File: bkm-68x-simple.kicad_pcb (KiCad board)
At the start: 2 copper layers, 230.4 x 233.5 mm, 250 parts, among them CN985 mezz-conn-02x50, CN986 mezz-conn-02x50, J1 PR_R, J10 TP_VIDEO_OE, J11 TP_VSYNC, J12 JTAG, J13 PR_R_OUT, J14 VSYNC_DISCRETE, J15 Y_G_OUT, J16 PB_B_OUT, J17 EXT_SYNC_OUT, J18 Conn_01x02_Male, J19 TP_NORM_Y_G, J2 Y_G, J20 TP_RGB_COMP_X, J21 TP_HD_SD_X, J3 PB_B, J4 EXT_SYNC, J401 JTAG, J5 TP_Y_G, J6 TP_PB_B, J601 Conn_01x07_Male, J7 TP_PR_R, J8 TP_HSYNC, J9 TP_INT_EXT_SYNC, Q1 MMBT3904, Q2 MMBT3904, SW1 FORCE_VIDEO, SW2 FORCE_VIDEO, SW3 PR_R_TERM, SW4 Y_G_TERM, SW5 PB_B_TERM, SW6 EXT_SYNC_TERM, U1 ADG1611BCPZ, U10 74LVC541A, U101 NCV8164ASN120T1G, U102 BD33HC0WEFJ-E2, U11 74LVC2G34, U12 TC7SZ125FU, U13 LM2990SX-5.0, U14 BA50BC0FP-E2, U16 SN74LVC1G14DBV, U17 ISL4089, U19 74LVC2G34, U2 THS7374, U3 ISL59885, U301 FSA2257MUX, U5 74LVC14A, U6 74LVC14A, U601 W25Q128JVS, U7 74LVC14A, U8 TC7WH125, U801 T8Q144, U9 KC2520Z50

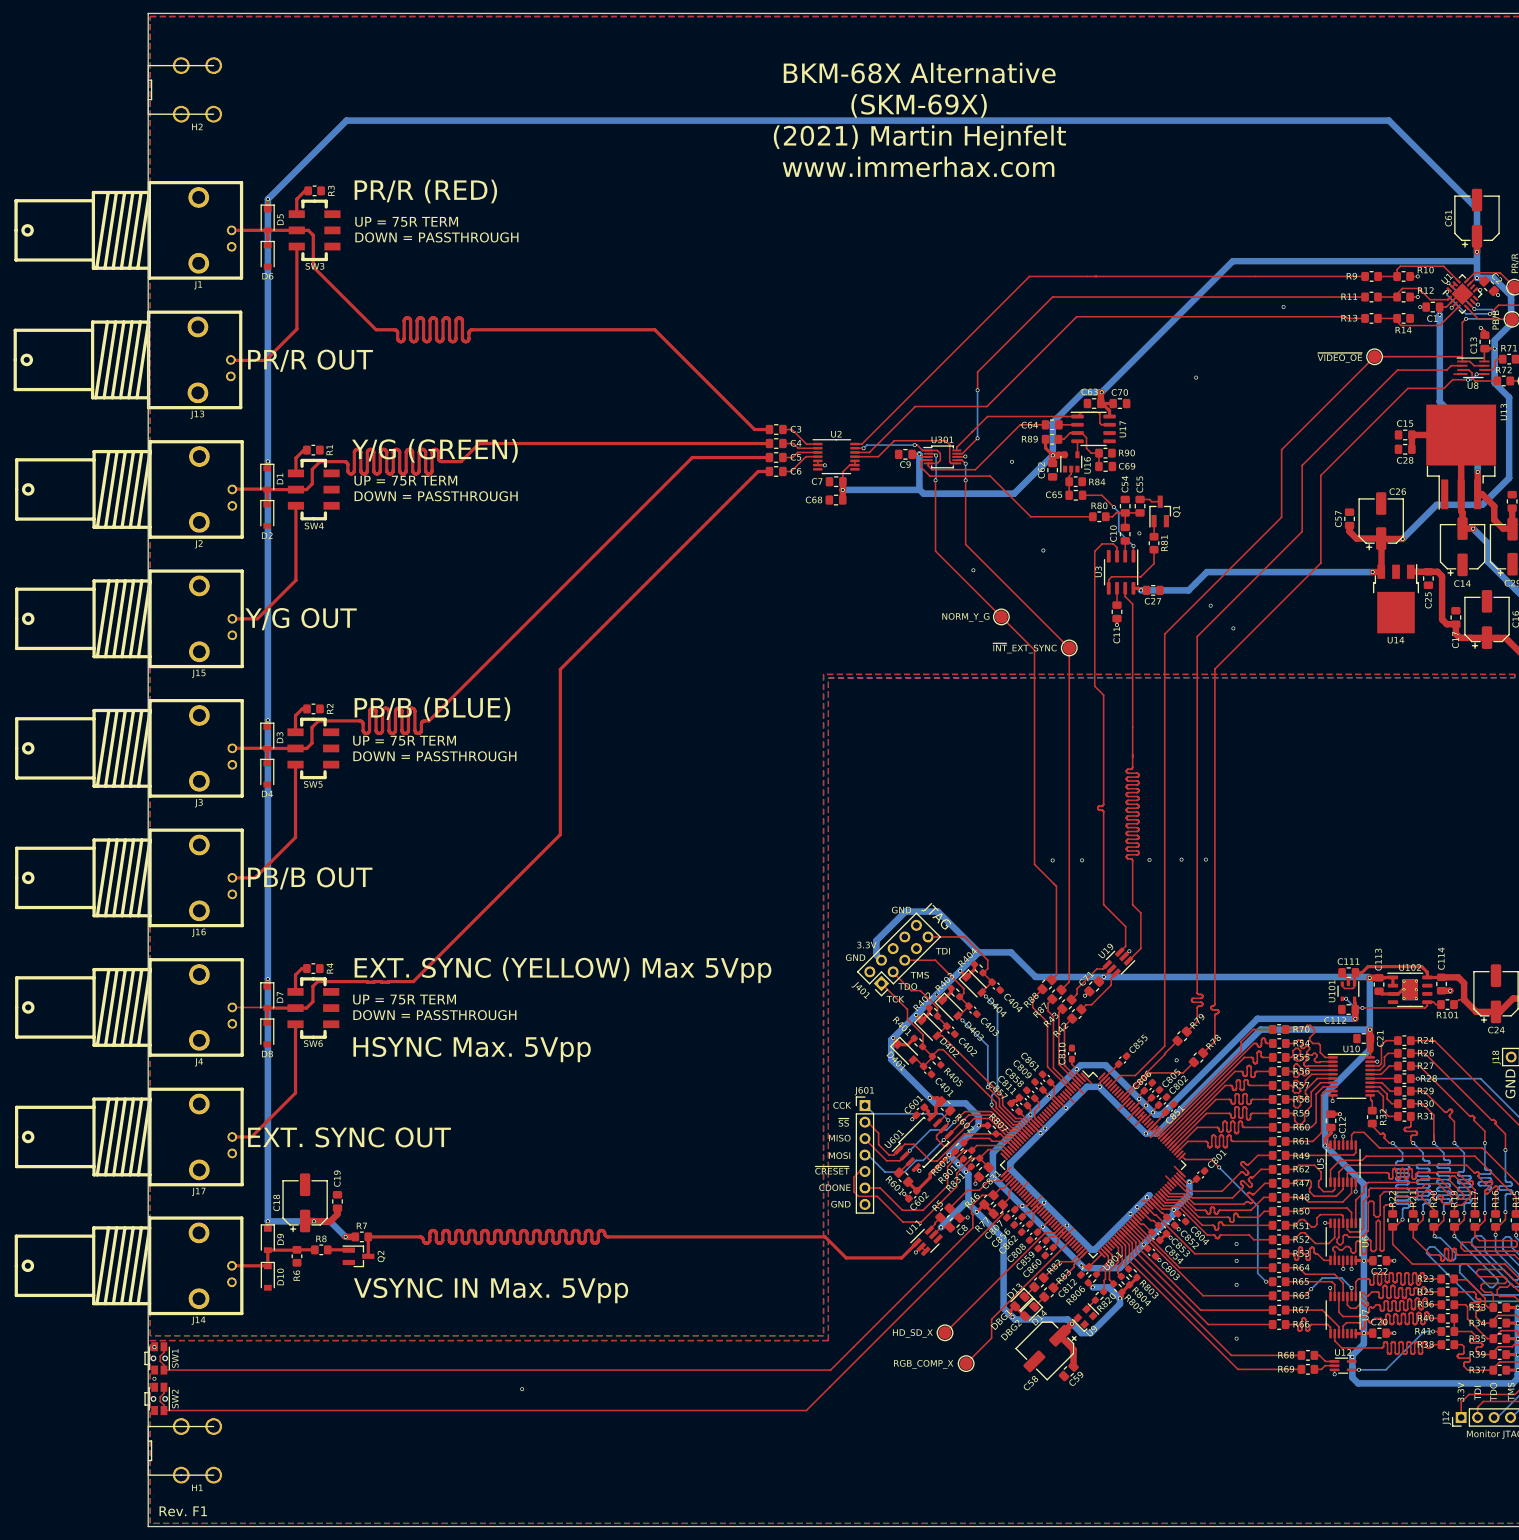
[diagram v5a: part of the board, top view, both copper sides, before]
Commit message: Added vsync out
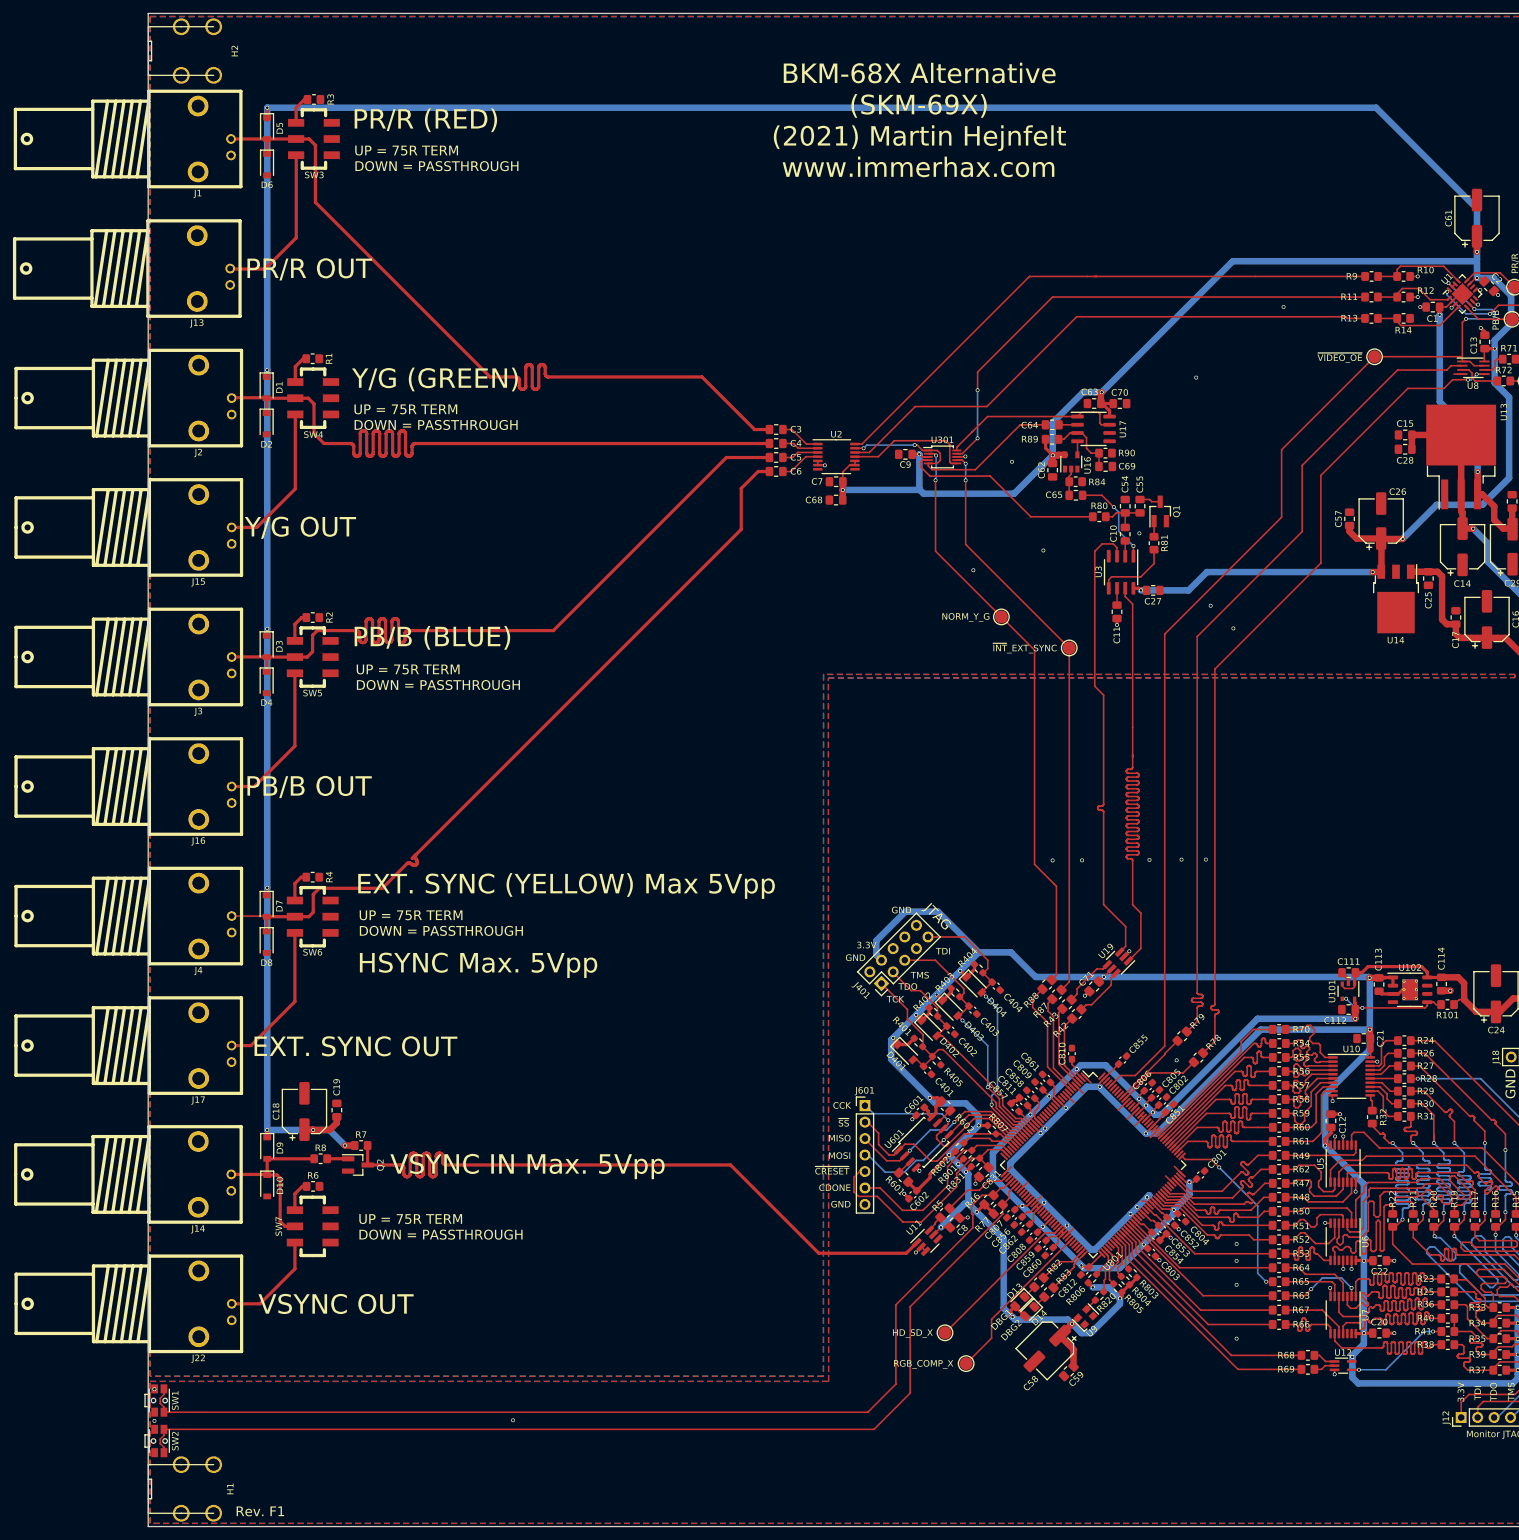
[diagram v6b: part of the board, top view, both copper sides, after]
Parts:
- added J22: VSYNC_DISCRETE_OUT, BNC-THT:BNC-THT, F.Cu at (59.3, 232.3)
- added SW7: EXT_SYNC_TERM, JS202011SCQN:JS202011SCQN, F.Cu at (76.9, 220.4)
- moved D4 14.1 mm to (69.8, 136.5)
- moved D8 14.1 mm to (69.8, 176.5)
- moved D2 14.1 mm to (69.8, 96.5)
- moved J13 14.1 mm to (59.1, 72.6)
- moved J15 14.1 mm to (59.3, 112.5)
- moved J2 14.1 mm to (59.3, 92.6)
- moved R1 14.1 mm to (76.9, 86.5)
- moved SW4 14.1 mm to (77.0, 92.6)
- moved D5 14.1 mm to (69.9, 50.9)
- moved D6 14.1 mm to (69.9, 56.5)
- moved R3 14.1 mm to (77.1, 46.5)
- moved C18 14.1 mm to (75.7, 202.7)
- moved C19 14.1 mm to (80.7, 202.4)
- moved D1 14.1 mm to (69.8, 90.9)
- moved D10 14.1 mm to (69.9, 214.1)
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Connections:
- R6 pad 1: Net-(D10-Pad1) -> Net-(R6-Pad1)
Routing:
- net VSYNC_DISCRETE_IN: track 133.1 -> 113.0 mm
- net Net-(J22-Pad1): track 0.00 -> 16.0 mm
- net Y_G_IN: track 136.1 -> 122.1 mm
- net PR_R_IN: track 136.3 -> 122.3 mm
- net PB_B_IN: track 136.1 -> 122.1 mm
- net EXT_SYNC_IN: track 136.1 -> 122.1 mm
- net Net-(D10-Pad1): track 15.3 -> 26.8 mm
- net FORCE_VIDEO: track 149.2 -> 159.0 mm
- net FORCE_VIDEO2: track 151.3 -> 160.4 mm
- net Net-(R6-Pad1): track 0.00 -> 4.80 mm
- net +5VA: track 656.8 -> 652.7 mm
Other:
- board text added: "VSYNC OUT"
